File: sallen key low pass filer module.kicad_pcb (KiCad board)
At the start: 2 copper layers, 27.4 x 13.7 mm, 17 parts, among them P1 CONN_01X04, P2 CONN_01X04, U1 AD8692

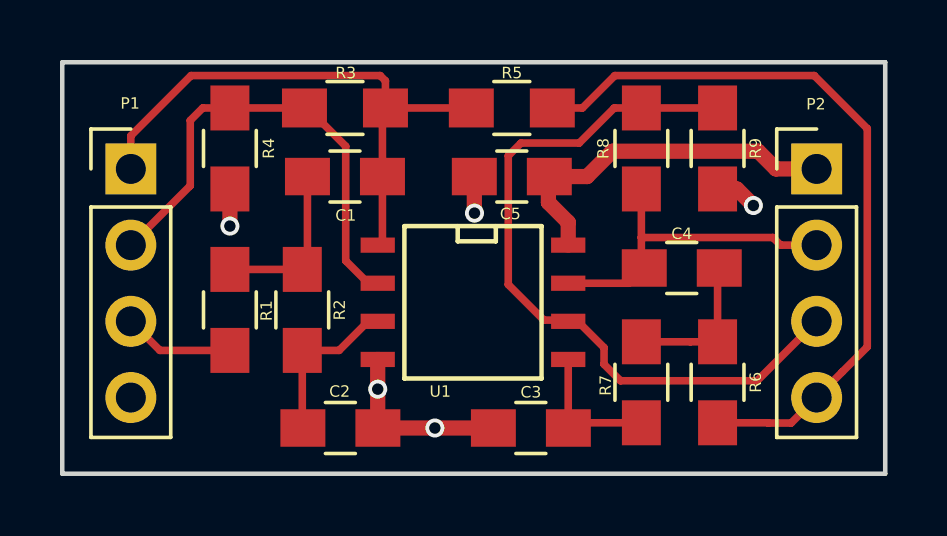
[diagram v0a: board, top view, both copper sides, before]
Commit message: silk screen edits
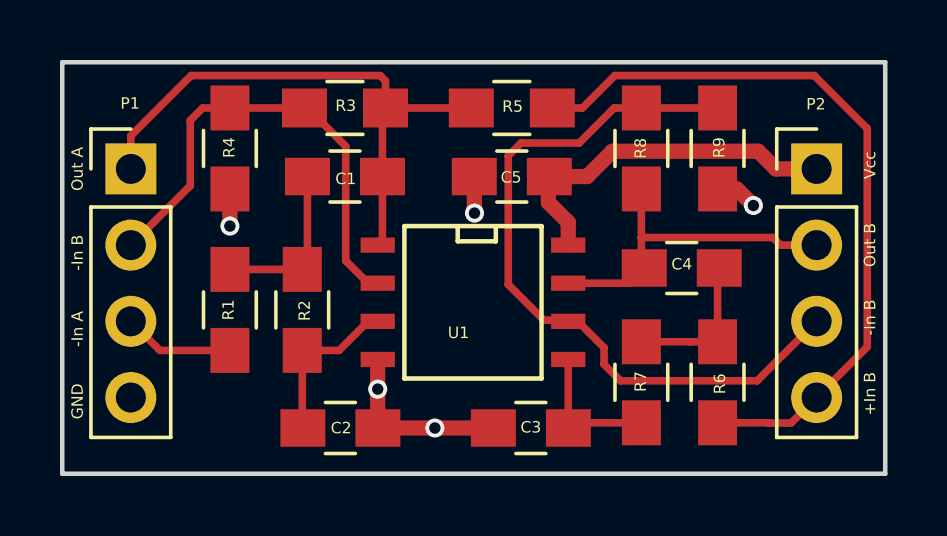
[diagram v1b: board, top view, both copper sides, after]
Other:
- board text added: "+In B"
- board text added: "-In A"
- board text added: "-In B"
- board text added: "GND"
- board text added: "Out A"
- board text added: "Out B"
- board text added: "Vcc"
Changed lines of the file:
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@@
   (general
     (links 32)
-    (no_connects 24)
-    (area 129.718999 97.968999 157.301001 111.835001)
+    (no_connects 0)
+    (area 126.917667 96.639 160.102334 113.015)
     (thickness 1.6)
-    (drawings 4)
+    (drawings 12)
     (tracks 99)
     (zones 0)
@@
     (47 F.CrtYd user)
     (48 B.Fab user)
-    (49 F.Fab user)
+    (49 F.Fab user hide)
   )
   (setup
@@
     (visible_elements 7FFFFF7F)
     (pcbplotparams
-      (layerselection 0x00030_80000001)
-      (usegerberextensions false)
+      (layerselection 0x010f0_80000001)
+      (usegerberextensions true)
       (excludeedgelayer true)
-      (linewidth 0.100000)
+      (linewidth 2.000000)
       (plotframeref false)
       (viasonmask false)
@@
       (outputformat 1)
       (mirror false)
-      (drillshape 1)
+      (drillshape 0)
       (scaleselection 1)
-      (outputdirectory ""))
+      (outputdirectory ../))
   )
   (net 0 "")
@@
     (tags "capacitor 0805")
     (attr smd)
-    (fp_text reference C1 (at 0.0254 1.2954) (layer F.SilkS)
+    (fp_text reference C1 (at 0.0254 0.0762) (layer F.SilkS)
       (effects (font (size 0.381 0.381) (thickness 0.0635)))
     )
@@
     (tags "capacitor 0805")
     (attr smd)
-    (fp_text reference C2 (at -0.0254 -1.2192) (layer F.SilkS)
+    (fp_text reference C2 (at 0.0254 0) (layer F.SilkS)
       (effects (font (size 0.381 0.381) (thickness 0.0635)))
     )
@@
     (tags "capacitor 0805")
     (attr smd)
-    (fp_text reference C3 (at 0 1.1938 180) (layer F.SilkS)
+    (fp_text reference C3 (at 0 0.0254 180) (layer F.SilkS)
       (effects (font (size 0.381 0.381) (thickness 0.0635)))
     )
@@
     (tags "capacitor 0805")
     (attr smd)
-    (fp_text reference C4 (at 0 1.143 180) (layer F.SilkS)
+    (fp_text reference C4 (at 0 0.127 180) (layer F.SilkS)
       (effects (font (size 0.381 0.381) (thickness 0.0635)))
     )
@@
     (tags "resistor 0805")
     (attr smd)
-    (fp_text reference R1 (at 0.0254 -1.2192 270) (layer F.SilkS)
+    (fp_text reference R1 (at 0 0.0508 270) (layer F.SilkS)
       (effects (font (size 0.381 0.381) (thickness 0.0635)))
     )
@@
     (tags "resistor 0805")
     (attr smd)
-    (fp_text reference R2 (at 0 1.2446 90) (layer F.SilkS)
+    (fp_text reference R2 (at -0.0254 0.0762 90) (layer F.SilkS)
       (effects (font (size 0.381 0.381) (thickness 0.0635)))
     )
@@
     (tags "resistor 0805")
     (attr smd)
-    (fp_text reference R3 (at -0.0254 1.1684 180) (layer F.SilkS)
+    (fp_text reference R3 (at -0.0254 0.0762 180) (layer F.SilkS)
       (effects (font (size 0.381 0.381) (thickness 0.0635)))
     )
@@
     (tags "resistor 0805")
     (attr smd)
-    (fp_text reference R4 (at -0.0038 -1.2954 270) (layer F.SilkS)
+    (fp_text reference R4 (at -0.0292 0.0254 270) (layer F.SilkS)
       (effects (font (size 0.381 0.381) (thickness 0.0635)))
     )
@@
     (tags "resistor 0805")
     (attr smd)
-    (fp_text reference R5 (at 0 1.1684 180) (layer F.SilkS)
+    (fp_text reference R5 (at -0.0254 0.0508 180) (layer F.SilkS)
       (effects (font (size 0.381 0.381) (thickness 0.0635)))
     )
@@
     (tags "resistor 0805")
     (attr smd)
-    (fp_text reference R6 (at 0 -1.27 270) (layer F.SilkS)
+    (fp_text reference R6 (at 0.0508 -0.0762 270) (layer F.SilkS)
       (effects (font (size 0.381 0.381) (thickness 0.0635)))
     )
@@
     (tags "resistor 0805")
     (attr smd)
-    (fp_text reference R7 (at -0.1016 -1.1938 90) (layer F.SilkS)
+    (fp_text reference R7 (at 0.0254 -0.0254 90) (layer F.SilkS)
       (effects (font (size 0.381 0.381) (thickness 0.0635)))
     )
@@
     (tags "resistor 0805")
     (attr smd)
-    (fp_text reference R8 (at 0 -1.27 90) (layer F.SilkS)
+    (fp_text reference R8 (at 0.0038 -0.0254 90) (layer F.SilkS)
       (effects (font (size 0.381 0.381) (thickness 0.0635)))
     )
@@
     (tags "resistor 0805")
     (attr smd)
-    (fp_text reference R9 (at -0.0038 -1.27 270) (layer F.SilkS)
+    (fp_text reference R9 (at -0.0292 -0.0508 270) (layer F.SilkS)
       (effects (font (size 0.381 0.381) (thickness 0.0635)))
     )
@@
     (tags "CMS SOJ")
     (attr smd)
-    (fp_text reference U1 (at 2.9718 1.0922 360) (layer F.SilkS)
+    (fp_text reference U1 (at 1.016 0.4826 360) (layer F.SilkS)
       (effects (font (size 0.381 0.381) (thickness 0.0635)))
     )
@@
     (tags "capacitor 0805")
     (attr smd)
-    (fp_text reference C5 (at 0.0508 -1.2446 180) (layer F.SilkS)
+    (fp_text reference C5 (at 0.0254 -0.0254 180) (layer F.SilkS)
       (effects (font (size 0.381 0.381) (thickness 0.0635)))
     )
@@
     )
   )
+  (gr_text "Out A" (at 130.302 101.6 90) (layer F.SilkS)
+    (effects (font (size 0.381 0.381) (thickness 0.0635)))
+  )
+  (gr_text "-In B" (at 130.302 104.394 90) (layer F.SilkS)
+    (effects (font (size 0.381 0.381) (thickness 0.0635)))
+  )
+  (gr_text "-In A" (at 130.302 106.934 90) (layer F.SilkS)
+    (effects (font (size 0.381 0.381) (thickness 0.0635)))
+  )
+  (gr_text GND (at 130.302 109.347 90) (layer F.SilkS)
+    (effects (font (size 0.381 0.381) (thickness 0.0635)))
+  )
+  (gr_text "+In B" (at 156.718 109.093 90) (layer F.SilkS)
+    (effects (font (size 0.381 0.381) (thickness 0.0635)))
+  )
+  (gr_text "-In B" (at 156.718 106.553 90) (layer F.SilkS)
+    (effects (font (size 0.381 0.381) (thickness 0.0635)))
+  )
+  (gr_text "Out B" (at 156.718 104.14 90) (layer F.SilkS)
+    (effects (font (size 0.381 0.381) (thickness 0.0635)))
+  )
+  (gr_text Vcc (at 156.718 101.473 90) (layer F.SilkS)
+    (effects (font (size 0.381 0.381) (thickness 0.0635)))
+  )
   (gr_line (start 129.794 98.044) (end 129.794 111.76) (layer Edge.Cuts) (width 0.15))
